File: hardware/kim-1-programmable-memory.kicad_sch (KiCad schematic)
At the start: 20 parts, among them J1 Conn_02x01, J3 EDGE_CONN, Q1 DMG2305UX, SW1 RESET, U1 74LVC541, U2 74LVC541, U3 74LVC245, U4 74LVC1G04, U6 74LVC1G38, U7 74LVC1G27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

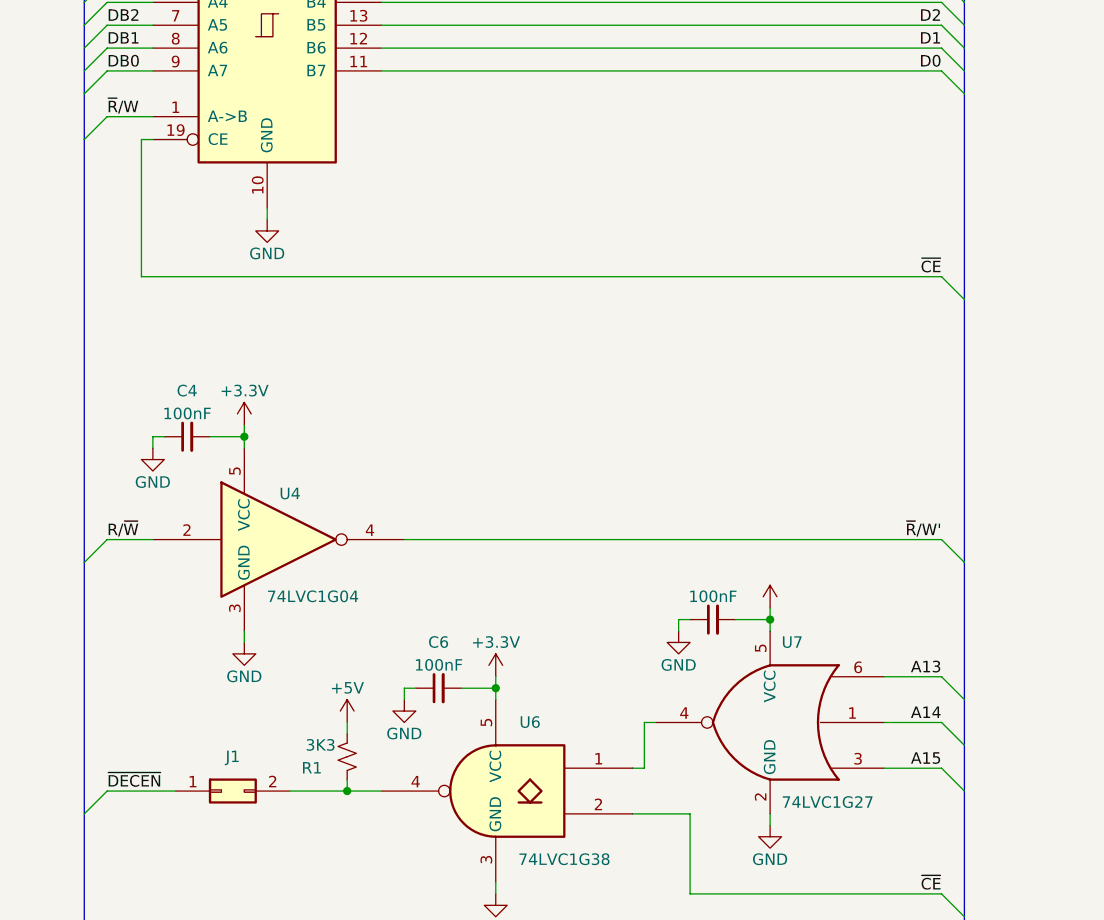
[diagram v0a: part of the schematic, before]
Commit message: Add pull-up resistor to OE
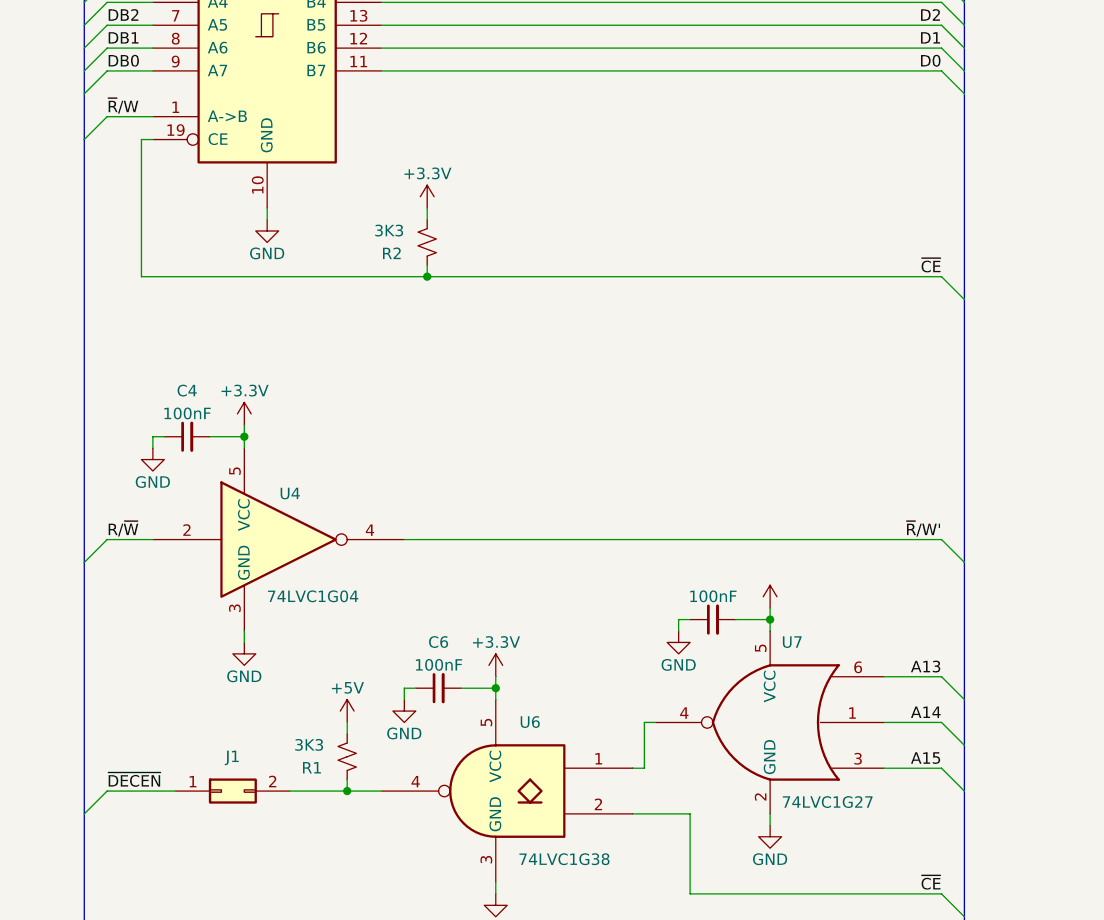
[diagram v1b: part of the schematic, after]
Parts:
- added R2: 3K3, Resistor_SMD:R_0603_1608Metric_Pad0.98x0.95mm_HandSolder, symbol Device:R_Small_US
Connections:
- net +3.3V: now also R2.2
- net ~{CE}: now also R2.1
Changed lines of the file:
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@@
   (junction (at 63.5 91.44) (diameter 0) (color 0 0 0 0)
+  )
+  (junction (at 81.28 214.63) (diameter 0) (color 0 0 0 0)
   )
   (no_connect (at 66.04 314.96))
@@
     (stroke (width 0) (type default))
   )
+  (wire (pts (xy 81.28 214.63) (xy 138.43 214.63))
+    (stroke (width 0) (type default))
+  )
   (wire (pts (xy 238.76 127) (xy 248.92 127))
     (stroke (width 0) (type default))
@@
     (stroke (width 0) (type default))
   )
+  (wire (pts (xy 81.28 207.01) (xy 81.28 208.28))
+    (stroke (width 0) (type default))
+  )
   (bus (pts (xy 140.97 133.35) (xy 140.97 130.81))
     (stroke (width 0) (type default) (color 194 0 194 1))
@@
     (stroke (width 0) (type default))
   )
+  (wire (pts (xy 81.28 213.36) (xy 81.28 214.63))
+    (stroke (width 0) (type default))
+  )
   (bus (pts (xy 190.5 160.02) (xy 190.5 162.56))
     (stroke (width 0) (type default) (color 194 0 194 1))
   )
-  (wire (pts (xy 49.53 214.63) (xy 138.43 214.63))
+  (wire (pts (xy 49.53 214.63) (xy 81.28 214.63))
     (stroke (width 0) (type default))
   )
@@
         (path "/28bcec85-7402-427d-8d3e-a0bb63c896a8"
           (reference "SW1") (unit 1)
+        )
+      )
+    )
+  )
+  (symbol (lib_id "power:+3.3V") (at 81.28 207.01 0) (unit 1)
+    (in_bom yes) (on_board yes) (dnp no)
+    (property "Reference" "#PWR020" (at 81.28 210.82 0)
+      (effects (font (size 1.27 1.27)) hide)
+    )
+    (property "Value" "+3.3V" (at 81.28 203.2 0)
+      (effects (font (size 1.27 1.27)))
+    )
+    (property "Footprint" "" (at 81.28 207.01 0)
+      (effects (font (size 1.27 1.27)) hide)
+    )
+    (property "Datasheet" "" (at 81.28 207.01 0)
+      (effects (font (size 1.27 1.27)) hide)
+    )
+    (pin "1")
+    (instances
+      (project "kim-1-programmable-memory"
+        (path "/28bcec85-7402-427d-8d3e-a0bb63c896a8"
+          (reference "#PWR020") (unit 1)
         )
       )
@@
         (path "/28bcec85-7402-427d-8d3e-a0bb63c896a8"
           (reference "#PWR013") (unit 1)
+        )
+      )
+    )
+  )
+  (symbol (lib_id "Device:R_Small_US") (at 81.28 210.82 0) (mirror x) (unit 1)
+    (in_bom yes) (on_board yes) (dnp no)
+    (property "Reference" "R2" (at 76.2 212.09 0)
+      (effects (font (size 1.27 1.27)) (justify left))
+    )
+    (property "Value" "3K3" (at 78.74 209.55 0)
+      (effects (font (size 1.27 1.27)) (justify right))
+    )
+    (property "Footprint" "Resistor_SMD:R_0603_1608Metric_Pad0.98x0.95mm_HandSolder" (at 81.28 210.82 0)
+      (effects (font (size 1.27 1.27)) hide)
+    )
+    (property "Datasheet" "~" (at 81.28 210.82 0)
+      (effects (font (size 1.27 1.27)) hide)
+    )
+    (pin "1")
+    (pin "2")
+    (instances
+      (project "kim-1-programmable-memory"
+        (path "/28bcec85-7402-427d-8d3e-a0bb63c896a8"
+          (reference "R2") (unit 1)
         )
       )
@@
       (effects (font (size 1.27 1.27)) (justify left))
     )
-    (property "Value" "3K3" (at 71.12 266.7 0)
+    (property "Value" "3K3" (at 69.85 266.7 0)
       (effects (font (size 1.27 1.27)) (justify right))
     )
